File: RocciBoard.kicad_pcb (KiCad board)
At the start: 2 copper layers, 99 x 54 mm, 196 parts, among them J1 Battery, J10 M3, J11 I2C6, J12 Power, J13 M2, J14 I2C7, J2 I2C0, J3 I2C1, J4 I2C2, J5 I2C3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

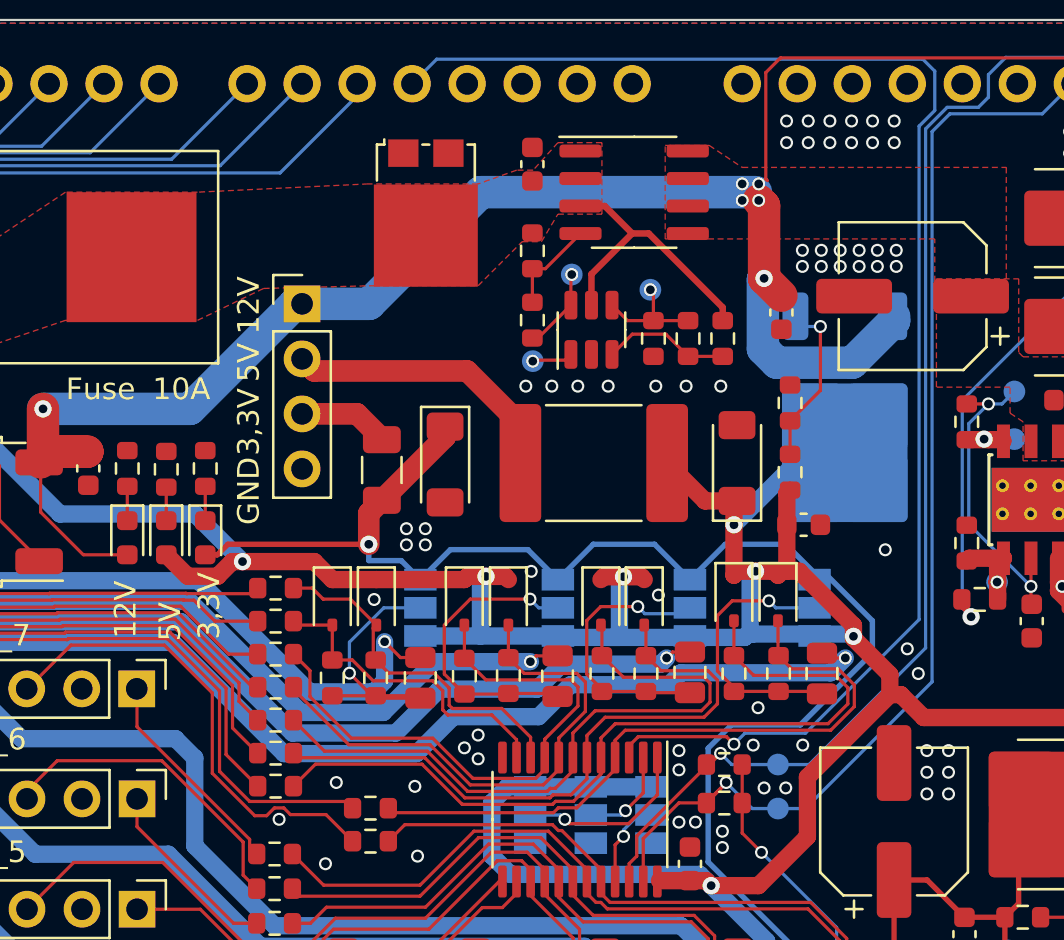
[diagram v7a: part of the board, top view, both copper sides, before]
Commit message: fix  #9 OVP 12V<->5V short circuit protection
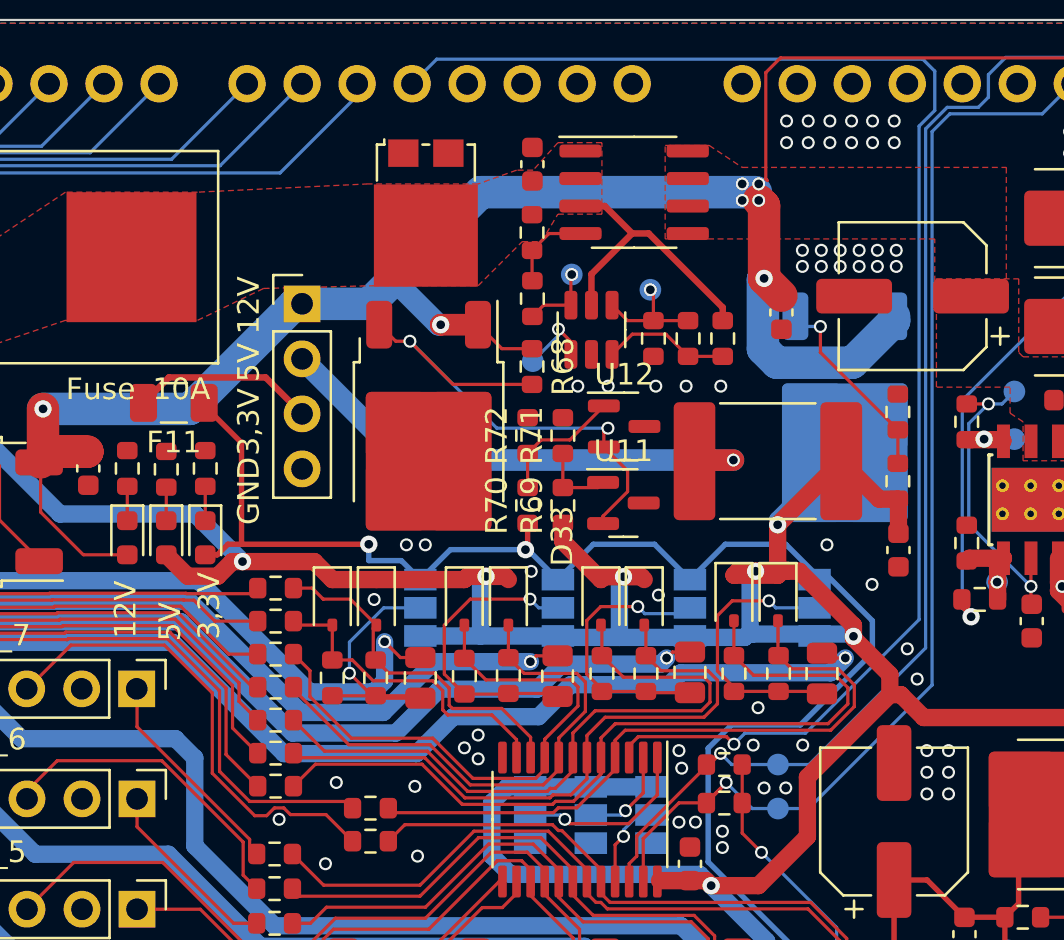
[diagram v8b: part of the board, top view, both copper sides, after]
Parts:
- removed D26: 3V4, Diode_SMD:D_MiniMELF
- removed D27: 5V1, Diode_SMD:D_MiniMELF
- added D33: BT137S-600E, Package_TO_SOT_SMD:TO-252-2, F.Cu at (174.0, 96.4)
- added R68: 1k, Resistor_SMD:R_0603_1608Metric, F.Cu at (178.8, 93.3)
- added R69: 1k5, Resistor_SMD:R_0603_1608Metric, F.Cu at (180.2, 99.7)
- added R70: 1k3, Resistor_SMD:R_0603_1608Metric, F.Cu at (178.6, 99.7)
- added R71: 1k, Resistor_SMD:R_0603_1608Metric, F.Cu at (180.2, 96.5)
- added R72: 2k, Resistor_SMD:R_0603_1608Metric, F.Cu at (178.6, 96.5)
- added U11: CJ431, Package_TO_SOT_SMD:SOT-23, F.Cu at (183.0, 99.6)
- added U12: CJ431, Package_TO_SOT_SMD:SOT-23, F.Cu at (183.0, 96.1)
- moved F11 10.1 mm to (162.2, 95.0), turned to 180 degrees
- moved F9 8.04 mm to (189.7, 97.7)
- moved R66 4.99 mm to (195.7, 98.6)
- moved R67 4.99 mm to (195.7, 95.4)
- moved C23 4.53 mm to (195.7, 101.8), turned to -90 degrees
- moved R65 1.00 mm to (178.8, 90.2)
- moved R14 0.84 mm to (178.8, 87.1)
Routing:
- net Net-(D33-G): track 0.00 -> 24.4 mm, vias 0 -> 2
- net Net-(J12-Pin_2): track 13.1 -> 23.7 mm, vias 0 -> 1
- net +12VA: track 148.5 -> 156.3 mm, vias 6 -> 7
- net Net-(U12-REF): track 0.00 -> 6.00 mm
- net Net-(J12-Pin_3): track 4.21 -> 8.51 mm
- net +5V: track 289.6 -> 293.3 mm
- net Net-(U11-REF): track 0.00 -> 3.53 mm
- net +3V3: track 120.3 -> 121.9 mm, vias 3 -> 4
- net Net-(U4-OUTA): track 1.89 -> 3.37 mm
- net Net-(U10-ADJ): track 7.83 -> 9.15 mm
- net GND: vias 119 -> 116
